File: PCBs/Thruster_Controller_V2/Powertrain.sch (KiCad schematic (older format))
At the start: 53 parts, among them Q1 SIZF906DT, Q2 SIZF906DT, Q3 SIZF906DT, U3 DRV8320S

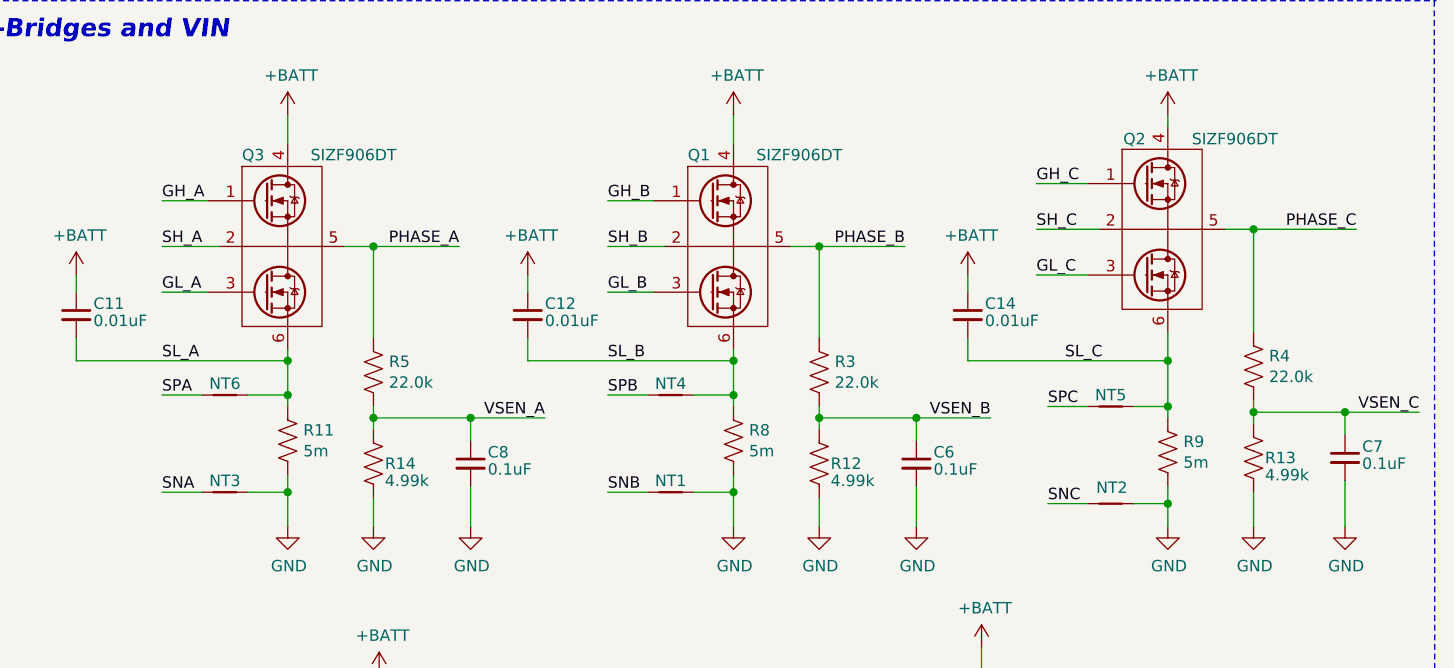
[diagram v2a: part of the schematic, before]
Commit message: Restart
- Semester is over, back to work
- Starting by ripping up all tracks
- Component placement for powertrain, still need to look at feedback signals
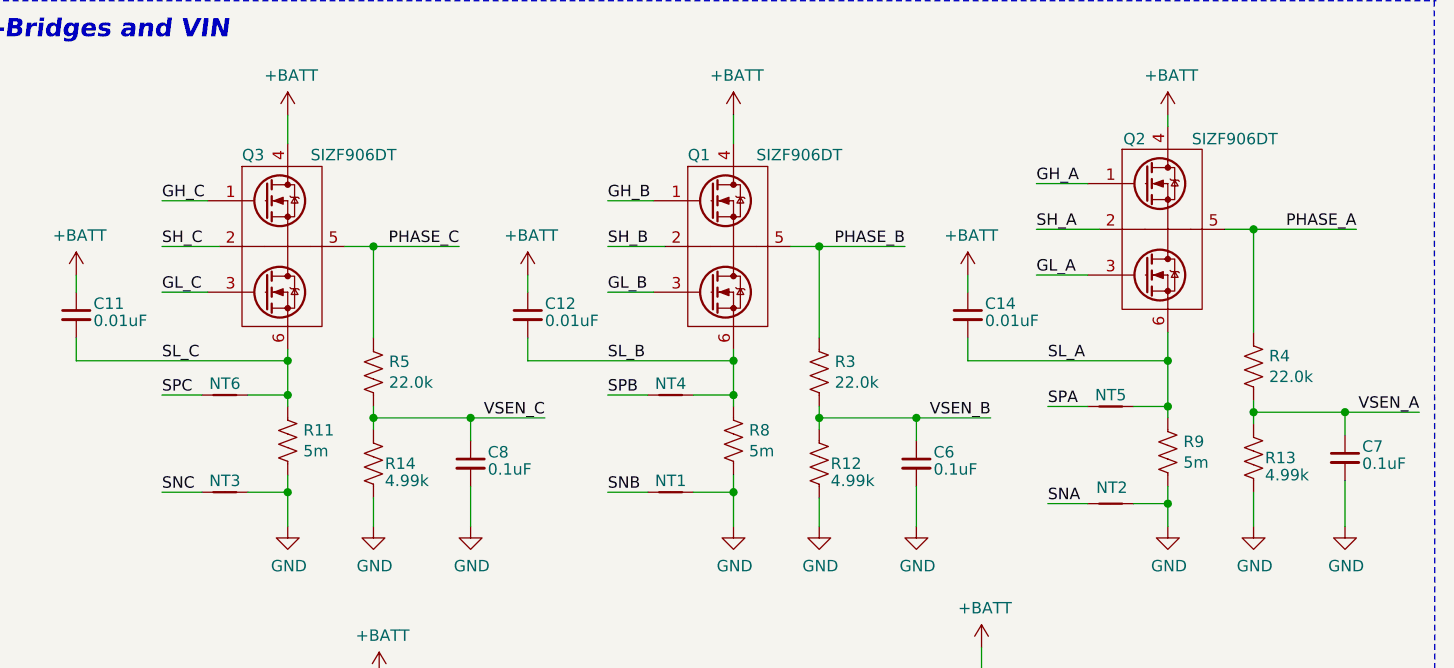
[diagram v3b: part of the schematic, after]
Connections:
- net GH_A: now also Q2.1 (GHS/G1); no longer Q3.1 (GHS/G1)
- net GH_C: now also Q3.1 (GHS/G1); no longer Q2.1 (GHS/G1)
- net GL_A: now also Q2.3 (GLS/G2); no longer Q3.3 (GLS/G2)
- net GL_C: now also Q3.3 (GLS/G2); no longer Q2.3 (GLS/G2)
- net Phase_A: now also Q2.5 (VSW/S1-D2), R4.1; no longer Q3.5 (VSW/S1-D2), R5.1
- net Phase_C: now also Q3.5 (VSW/S1-D2), R5.1; no longer Q2.5 (VSW/S1-D2), R4.1
- net SH_A: now also Q2.2 (Return/S1); no longer Q3.2 (Return/S1)
- net SH_C: now also Q3.2 (Return/S1); no longer Q2.2 (Return/S1)
- net SL_A: now also C14.2, NT5.2, Q2.6 (GND/S2), R9.1; no longer C11.2, NT6.2, Q3.6 (GND/S2), R11.1
- net SL_C: now also C11.2, NT6.2, Q3.6 (GND/S2), R11.1; no longer C14.2, NT5.2, Q2.6 (GND/S2), R9.1
- net SPA: now also NT5.1; no longer NT6.1
- net SPC: now also NT6.1; no longer NT5.1
- net VSEN_A: now also C7.1, R13.1, R4.2; no longer C8.1, R14.1, R5.2
- net VSEN_C: now also C8.1, R14.1, R5.2; no longer C7.1, R13.1, R4.2
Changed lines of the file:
@@
 	1    0    0    -1
 $EndComp
-Text Label 5550 1375 0    50   ~ 0
+Text Label 9375 1300 0    50   ~ 0
 GH_A
-Text Label 5550 1775 0    50   ~ 0
+Text Label 9375 1700 0    50   ~ 0
 GL_A
 $Comp
@@
 	1    0    0    -1
 $EndComp
-Text Label 5550 1575 0    50   ~ 0
+Text Label 9375 1500 0    50   ~ 0
 SH_A
-Text Label 5550 2075 0    50   ~ 0
+Text Label 9425 2075 0    50   ~ 0
 SL_A
-Text Label 5550 2225 0    50   ~ 0
+Text Label 9425 2275 0    50   ~ 0
 SPA
 $Comp
@@
 	1    0    0    -1
 $EndComp
-Text Label 6850 1575 2    50   ~ 0
+Text Label 10775 1500 2    50   ~ 0
 PHASE_A
 Wire Wire Line
@@
 	1    0    0    -1
 $EndComp
-Text Label 7225 2325 2    50   ~ 0
+Text Label 11050 2300 2    50   ~ 0
 VSEN_A
 Wire Wire Line
@@
 Text Label 8800 1575 2    50   ~ 0
 PHASE_B
-Text Label 10775 1500 2    50   ~ 0
+Text Label 6850 1575 2    50   ~ 0
 PHASE_C
-Text Label 11050 2300 2    50   ~ 0
+Text Label 7225 2325 2    50   ~ 0
 VSEN_C
 Text Label 7500 1375 0    50   ~ 0
@@
 Text Label 7500 2650 0    50   ~ 0
 SNB
-Text Label 9375 1300 0    50   ~ 0
+Text Label 5550 1375 0    50   ~ 0
 GH_C
-Text Label 9375 1500 0    50   ~ 0
+Text Label 5550 1575 0    50   ~ 0
 SH_C
-Text Label 9375 1700 0    50   ~ 0
+Text Label 5550 1775 0    50   ~ 0
 GL_C
-Text Label 9500 2075 0    50   ~ 0
+Text Label 5550 2075 0    50   ~ 0
 SL_C
-Text Label 9425 2275 0    50   ~ 0
+Text Label 5550 2225 0    50   ~ 0
 SPC
-Text Label 9425 2700 0    50   ~ 0
+Text Label 5550 2650 0    50   ~ 0
 SNC
 Wire Notes Line
@@
 	1    0    0    -1
 $EndComp
-Text Label 5550 2650 0    50   ~ 0
+Text Label 9425 2700 0    50   ~ 0
 SNA
 Wire Wire Line

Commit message: Schematic Work / BOM
- Double checking pinout
- Adding digikey PNs for all components, cannot do a mouser run for a small quantity (1-2 boards)
- Generated BOM
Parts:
- U3: Digikey (none) -> 296-50725-1-ND
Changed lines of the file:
@@
 F 2 "Housings_DFN_QFN:WQFN-32-1EP_5x5mm_Pitch0.5mm" H 2675 4000 79  0001 C CNN
 F 3 "http://www.ti.com/lit/ds/symlink/drv8323r.pdf?HQS=TI-null-null-mousermode-df-pf-null-wwe&DCM=yes&ref_url=https%3A%2F%2Fwww.mouser.ca%2F&distId=26" H 5125 5600 79  0001 C CNN
-F 4 "" H 4275 5450 79  0001 C CNN "Digikey"
+F 4 "296-50725-1-ND" H 4275 5450 79  0001 C CNN "Digikey"
 F 5 "595-DRV8320SRTVR" H 2775 3350 50  0001 C CNN "Mouser"
 	1    2775 3350

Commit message: Silk and touchups
- Updated aluminum poly cap, adjusted courtyard
- Fixed silkscreen
- Added more power planes near LDOs
- Cleaned up some routing, still need to have a gooood look before sending this off. But, its 99% ready to go!
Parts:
- C10, C13, C15: footprint Capacitors_SMD:CP_Elec_6.3x5.8 -> Thruster_Controller:CP_Elec_6.3x5.8
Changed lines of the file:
@@
 F 0 "C15" H 7765 3796 50  0000 L CNN
 F 1 "220uF" H 7765 3705 50  0000 L CNN
-F 2 "Capacitors_SMD:CP_Elec_6.3x5.8" H 7688 3600 50  0001 C CNN
+F 2 "Thruster_Controller:CP_Elec_6.3x5.8" H 7688 3600 50  0001 C CNN
 F 3 "~" H 7650 3750 50  0001 C CNN
 F 4 "565-APXJ160ARA221MF61GCT-ND" H 7650 3750 50  0001 C CNN "Digikey"
@@
 F 0 "C13" H 7290 3796 50  0000 L CNN
 F 1 "220uF" H 7290 3705 50  0000 L CNN
-F 2 "Capacitors_SMD:CP_Elec_6.3x5.8" H 7213 3600 50  0001 C CNN
+F 2 "Thruster_Controller:CP_Elec_6.3x5.8" H 7213 3600 50  0001 C CNN
 F 3 "~" H 7175 3750 50  0001 C CNN
 F 4 "565-APXJ160ARA221MF61GCT-ND" H 7175 3750 50  0001 C CNN "Digikey"
@@
 F 0 "C10" H 6840 3796 50  0000 L CNN
 F 1 "220uF" H 6840 3705 50  0000 L CNN
-F 2 "Capacitors_SMD:CP_Elec_6.3x5.8" H 6763 3600 50  0001 C CNN
+F 2 "Thruster_Controller:CP_Elec_6.3x5.8" H 6763 3600 50  0001 C CNN
 F 3 "~" H 6725 3750 50  0001 C CNN
 F 4 "565-APXJ160ARA221MF61GCT-ND" H 6725 3750 50  0001 C CNN "Digikey"

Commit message: Updated Footprints
- Moved over to the default KiCAD footprints, the rounded ones.
- Updated all 3D models as well
- Need to fix a bunch of DRC errors ;(
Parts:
- C1, C20, C5: footprint Capacitors_SMD:C_0603 -> Capacitor_SMD:C_0603_1608Metric
- C11, C12, C14, C17, C2, C24, C25, C26, C6, C7, C8, C9: footprint Capacitors_SMD:C_0402 -> Capacitor_SMD:C_0402_1005Metric
- D2: footprint LEDs:LED_0603 -> LED_SMD:LED_0603_1608Metric
- R1, R12, R13, R14, R15, R16, R17, R18, R2, R20, R21, R22, R23, R24, R3, R32, R33, R4, R5, R6: footprint Resistors_SMD:R_0402 -> Resistor_SMD:R_0402_1005Metric
- R10: footprint Resistors_SMD:R_0603 -> Resistor_SMD:R_0603_1608Metric
- R11, R8, R9: footprint Resistors_SMD:R_2512 -> Resistor_SMD:R_2512_6332Metric
- U3: footprint Housings_DFN_QFN:WQFN-32-1EP_5x5mm_Pitch0.5mm -> Package_DFN_QFN:WQFN-32-1EP_5x5mm_P0.5mm_EP3.1x3.1mm
